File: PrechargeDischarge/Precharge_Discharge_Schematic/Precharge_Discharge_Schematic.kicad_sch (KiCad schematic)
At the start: 121 parts, among them J1 MicroFit, J2 Mini-Fit_Jr_5566-04A, J3 Micro-Fit 43045-0212, K1 OMRON-G2RL-24, K2 G7L-2A-X-L, K3 Relay_SPST-NC, Q1 2N7002, Q2 MMBT3906, Q3 2N7002, Q4 PMOS, U1 TJA1051T-3, U10 LM393, U11 4N35, U2 SPAN02A-12, U3 Teensy4.0, U4 LM1117-5.0, U5 4N35, U6 4N35, U7 LM331, U8 LM331, U9 LM2904

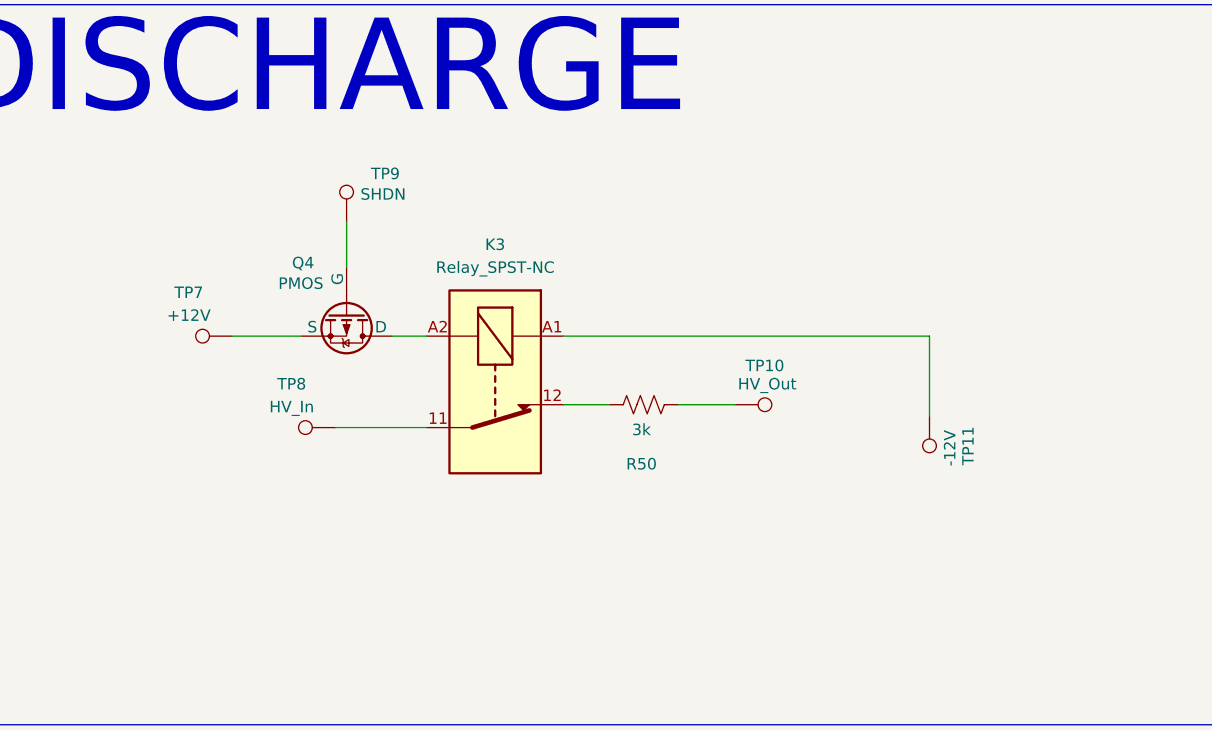
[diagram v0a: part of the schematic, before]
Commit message: added labels and pull down resistor
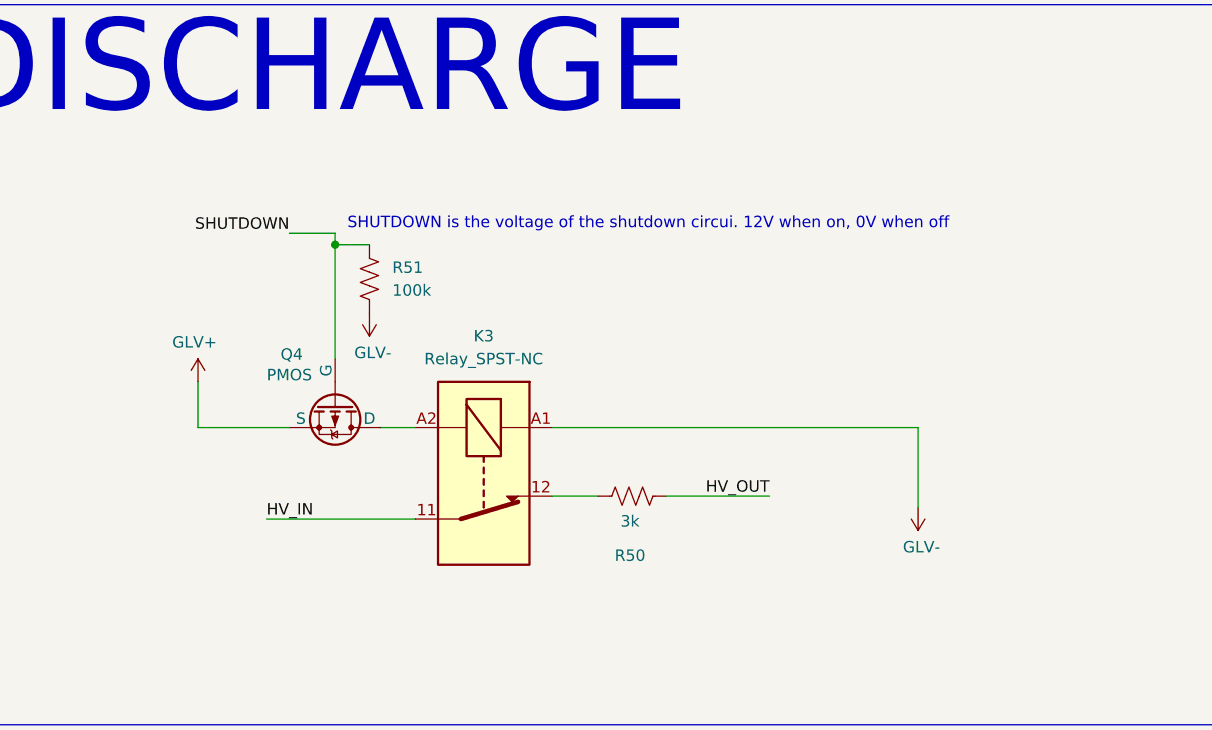
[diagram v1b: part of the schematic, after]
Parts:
- removed TP10: HV_Out, TestPoint:TestPoint_Loop_D1.80mm_Drill1.0mm_Beaded, symbol Connector:TestPoint
- removed TP11: -12V, TestPoint:TestPoint_Loop_D1.80mm_Drill1.0mm_Beaded, symbol Connector:TestPoint
- removed TP7: +12V, TestPoint:TestPoint_Loop_D1.80mm_Drill1.0mm_Beaded, symbol Connector:TestPoint
- removed TP8: HV_In, TestPoint:TestPoint_Loop_D1.80mm_Drill1.0mm_Beaded, symbol Connector:TestPoint
- removed TP9: SHDN, TestPoint:TestPoint_Loop_D1.80mm_Drill1.0mm_Beaded, symbol Connector:TestPoint
- added R51: 100k, symbol Device:R_US
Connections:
- net GLV+: now also Q4.3 (S)
- net GLV-: now also K3.A1, R51.2
- net SHUTDOWN: now reaches Q4.2 (G)
- net SHUTDOWN: now also R51.1
- net HV_IN: now reaches K3.11
- net HV_OUT: now reaches R50.2
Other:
- note added: "SHUTDOWN is the voltage of the shutdown circui. 12V when on, 0V when off"
- moved on the sheet: K3, Q4, R50
